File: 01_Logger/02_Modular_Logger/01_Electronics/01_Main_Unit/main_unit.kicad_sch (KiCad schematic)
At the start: 2 parts, among them J101 SFMC-107-01-L-D, J102 FTS-107-01-F-D

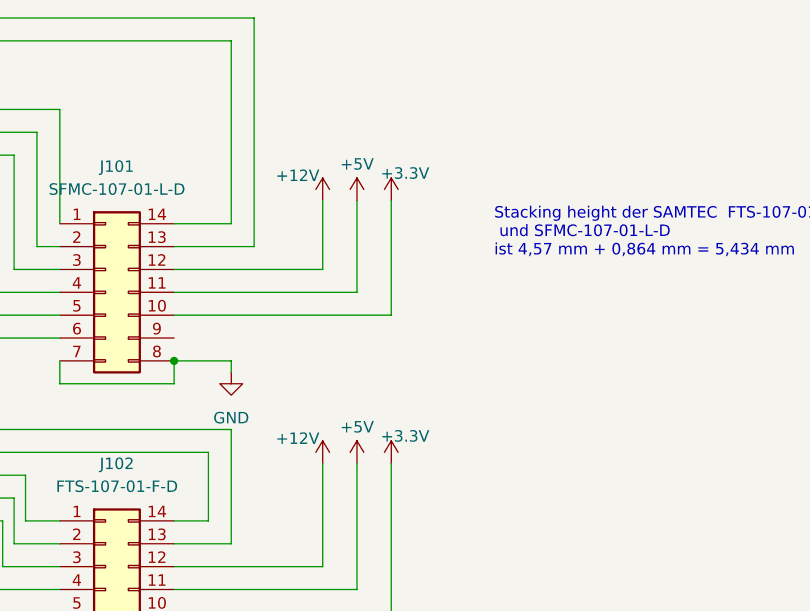
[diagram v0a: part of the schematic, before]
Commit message: update Electronics for Modular_Logger
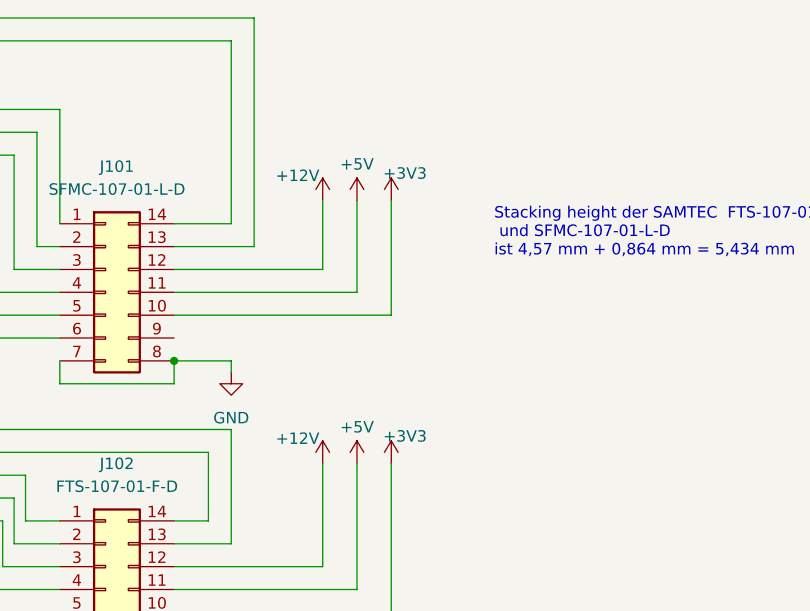
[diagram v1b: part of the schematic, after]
